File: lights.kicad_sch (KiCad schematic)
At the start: 25 parts

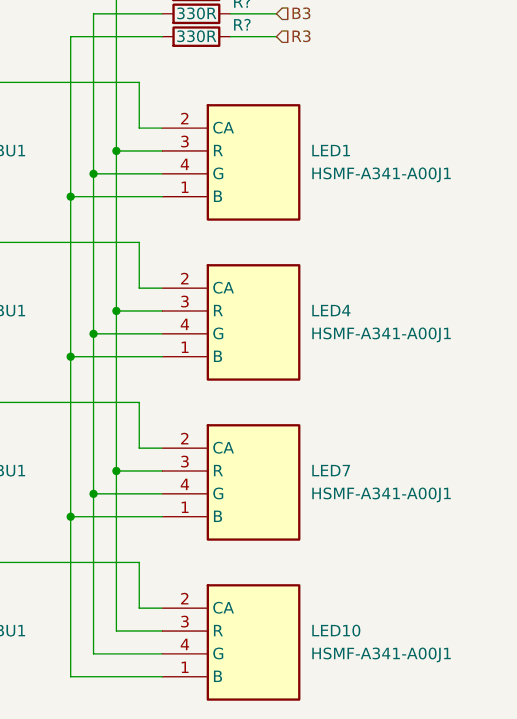
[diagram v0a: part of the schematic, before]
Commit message: Fix RGB LED part # should be ASMB-MTB1-0A3A2
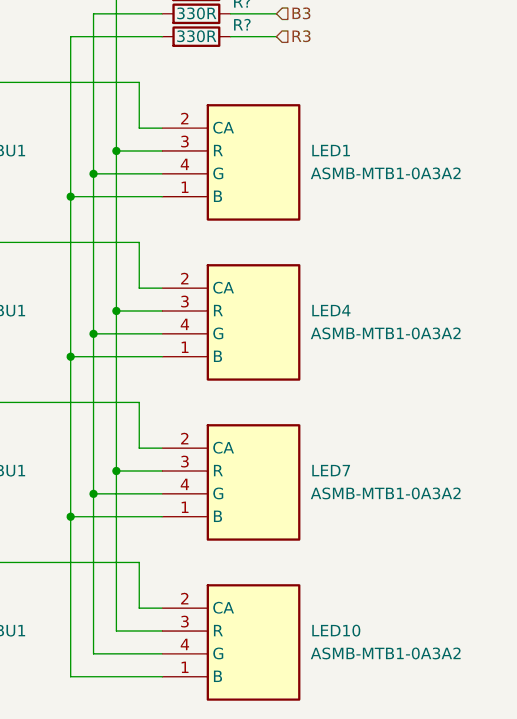
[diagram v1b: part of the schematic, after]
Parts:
- LED1, LED10, LED4, LED7: value HSMF-A341-A00J1 -> ASMB-MTB1-0A3A2
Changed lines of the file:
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@@
       (effects (font (size 1.27 1.27)) (justify left))
     )
-    (property "Value" "HSMF-A341-A00J1" (at 207.01 109.22 0)
+    (property "Value" "ASMB-MTB1-0A3A2" (at 207.01 109.22 0)
       (effects (font (size 1.27 1.27)) (justify left))
     )
@@
       (effects (font (size 1.27 1.27)) (justify left))
     )
-    (property "Value" "HSMF-A341-A00J1" (at 207.01 73.66 0)
+    (property "Value" "ASMB-MTB1-0A3A2" (at 207.01 73.66 0)
       (effects (font (size 1.27 1.27)) (justify left))
     )
@@
       (effects (font (size 1.27 1.27)) (justify left))
     )
-    (property "Value" "HSMF-A341-A00J1" (at 207.01 127 0)
+    (property "Value" "ASMB-MTB1-0A3A2" (at 207.01 127 0)
       (effects (font (size 1.27 1.27)) (justify left))
     )
@@
       (effects (font (size 1.27 1.27)) (justify left))
     )
-    (property "Value" "HSMF-A341-A00J1" (at 207.01 91.44 0)
-      (effects (font (size 1.27 1.27)) (justify left))
-    )
+    (property "Value" "ASMB-MTB1-0A3A2" (at 207.01 91.44 0)
+      (effects (font (size 1.27 1.27)) (justify left))
+    )
